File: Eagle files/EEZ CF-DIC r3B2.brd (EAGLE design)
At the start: 155 x 85 mm, 238 parts, among them IC1 MC79L05, IC2 LP2951, IC3 VIPer35L, IC4 SI8233BB-D-IS1, IC5 LM5041B, IC6 IR11688STRPBF, IC7 TL072, IC8 TL103W, IC9 TL431, P1 T910W-50K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

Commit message: X2 12V connector added
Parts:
- added X4: 39-28-1023, EEZ_Lib1:MINIFIT_5566-02A
- C4: value CY1Y-470P -> N.C.; device EEZ_Lib1:CY075-032X103 -> rcl:C0603
- C6: value N.C. -> CY1Y-470P; device rcl:C0603 -> EEZ_Lib1:CY075-032X103
- R2: value 220K -> 120R; device rcl:R1206 -> rcl:R0805
- R3: value 120R -> 220K; device rcl:R0805 -> rcl:R1206
- TP6: device EEZ_Lib1:TP_1.1MM_2 -> EEZ_Lib1:PCB_SHIELD_TAB
- TP7: device EEZ_Lib1:PCB_SHIELD_TAB -> EEZ_Lib1:TP_1.1MM_2
- X1: value 39-30-1039 -> B2B-ZR; device EEZ_Lib1:MINIFIT_39301039_CRE -> EEZ_Lib1:B2B-ZR
- X2: value 90136-1208 -> 39-30-1039; device con-molex:70543-08 -> EEZ_Lib1:MINIFIT_39301039_CRE
- X3: value 39-28-1023 -> 90136-1208; device EEZ_Lib1:MINIFIT_5566-02A -> con-molex:70543-08
- moved X2 146.6 mm to (145.0, 9.91), turned to 180 degrees
- moved R2 101.0 mm to (64.4, 83.4), flipped to the top, turned to 270 degrees
- moved R3 101.0 mm to (150.3, 30.3), flipped to the bottom, turned to 180 degrees
- moved X1 91.2 mm to (77.5, 71.2), turned to 270 degrees
- moved C4 79.1 mm to (78.1, 78.4), flipped to the bottom, turned to 180 degrees
- moved C6 69.6 mm to (143.0, 53.3), flipped to the top
- moved TP6 65.3 mm to (72.7, 39.5)
- moved TP8 38.4 mm to (34.3, 38.7)
- moved TP7 27.4 mm to (7.62, 44.5)
- moved X3 26.4 mm to (9.59, 66.1)
- moved C5 10.2 mm to (153.2, 53.3), turned to 0 degrees
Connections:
- net +12V: now also C4.1, X1.1; no longer C6.1
- net -9V: now also X3.8; no longer X2.8
- net 0V: now also C4.2, X1.2; no longer C6.2
- net DC_OUT: now also X3.3; no longer X2.3
- net FB: now also TP8.1; no longer TP7.1
- net GND: now also TP7.GND, X3.6, X4.2; no longer TP6.GND, X2.6, X3.2
- net ISO_FB: now also TP6.1; no longer TP8.1
- net N$140: now also R2.2; no longer R3.2
- net N$15: now also C6.2; no longer C5.2
- net N$24: now also C5.2; no longer C4.2
- net N$27: now also R2.1; no longer R3.1
- net N$28: now also X2.2; no longer X1.2
- net N$30: now also R3.2, X2.3; no longer R2.2, X1.3
- net N$33: now also R3.1; no longer R2.1
- net PE: now also C6.1, X2.1; no longer C4.1, X1.1
- net PREG_OUT+: now also TP7.TIP, X3.2, X4.1; no longer TP6.TIP, X2.2, X3.1
- net PWRGOOD: now also X3.4; no longer X2.4
- net U_MON: now also X3.1; no longer X2.1
- net V+: now also X3.5; no longer X2.5
- net V-: now also X3.7; no longer X2.7
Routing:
- net +12V: track 107.7 -> 114.1 mm
- net 0V: track 588.9 -> 591.1 mm
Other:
- board text added: "X3 connector"
- board text added: "X4"
- board text removed: "X2 connector"

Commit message: small changes on PCB, added alternative sync MOSFET in BOM
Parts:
- added C73: N.C., rcl:C0805
- C59: value 4n7/200V -> 100n/100V; device rcl:C1206 -> rcl:C0805
- C60, C64: value 100n -> 4n7/200V; device rcl:C0603 -> rcl:C1206
- C61: value 10u -> 100n; device rcl:C1210 -> rcl:C0603
- C62: value 100n -> 10u; device rcl:C0603 -> rcl:C1210
- C63: value 4n7/200V -> 100n; device rcl:C1206 -> rcl:C0603
- C66: value 100p -> 100n; device rcl:C0805 -> rcl:C0603
- C68: value 33n -> 100p
- C69: value 4u7 -> 33n; device EEZ_Lib1:EC1206 -> rcl:C0805
- C70: value 1u -> 4u7; device rcl:C0805 -> EEZ_Lib1:EC1206
- C71: value N.C. -> 1u
- moved C59 48.5 mm to (10.5, 44.5), turned to 180 degrees
- moved C62 44.9 mm to (33.3, 6.67), turned to 270 degrees
- moved C63 34.6 mm to (46.7, 49.5)
- moved C64 29.2 mm to (42.1, 15.2)
- moved C71 19.4 mm to (57.1, 33.9), turned to 0 degrees
- moved C66 11.7 mm to (47.2, 40.2), turned to 0 degrees
- moved R38 11.0 mm to (132.9, 75.9)
- moved R42 11.0 mm to (132.9, 71.1)
- moved C70 10.3 mm to (58.1, 44.2)
- moved C67 9.66 mm to (56.6, 47.2), turned to 270 degrees
- moved C60 8.81 mm to (39.4, 5.52), turned to 0 degrees
- moved C69 7.58 mm to (56.1, 36.9), turned to 270 degrees
- moved C65 5.86 mm to (52.6, 42.5)
- moved C68 3.15 mm to (59.1, 37.9), turned to 180 degrees
- moved C72 3.15 mm to (39.3, 41.8), turned to 270 degrees
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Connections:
- net FB: now also C72.2; no longer C71.2
- net GND: now also C66.2, C70.-, C71.2; no longer C69.-, C70.2
- net N$1: now also C67.2; no longer C66.2
- net N$10: now also C68.2; no longer C67.2
- net N$134: now also C67.1; no longer C66.1
- net N$17: now also C73.2; no longer C72.2
- net N$6: now also C62.1; no longer C60.1
- net N$66: now also C60.1; no longer C59.1
- net N$67: now also C64.1; no longer C63.1
- net N$7: now also C71.1; no longer C70.1
- net N$76: now also C69.1, C73.1; no longer C67.1, C71.1
- net N$9: now also C69.2; no longer C68.2
- net NFB_OFFSET: now also C70.+; no longer C69.+
- net PREG_OUT+: now also C59.1
- net V+: now also C63.1, C66.1; no longer C62.1, C65.1
- net V-: now also C65.1; no longer C64.1
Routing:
- net ULVO: track 67.0 -> 77.4 mm
- net DC_BUS: track 187.0 -> 179.3 mm
- net PE: track 189.6 -> 195.4 mm, vias 2 -> 3
- net GND: track 136.4 -> 137.9 mm
- net PREG_OUT+: track 56.4 -> 55.2 mm
- net N$7: track 67.3 -> 66.4 mm
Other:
- board text added: "C73"

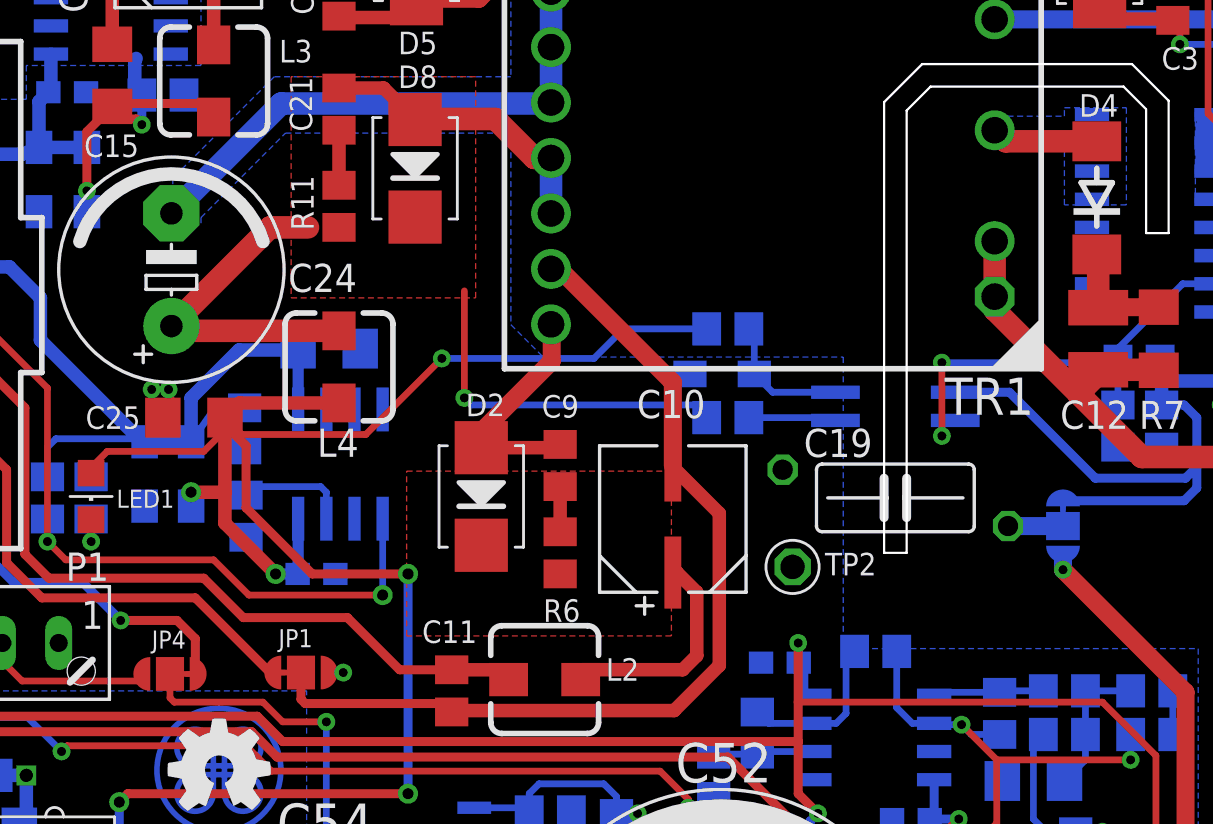
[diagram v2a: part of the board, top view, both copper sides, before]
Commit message: fixed .sch - .brd inconsistency reported by Eagle 7.x
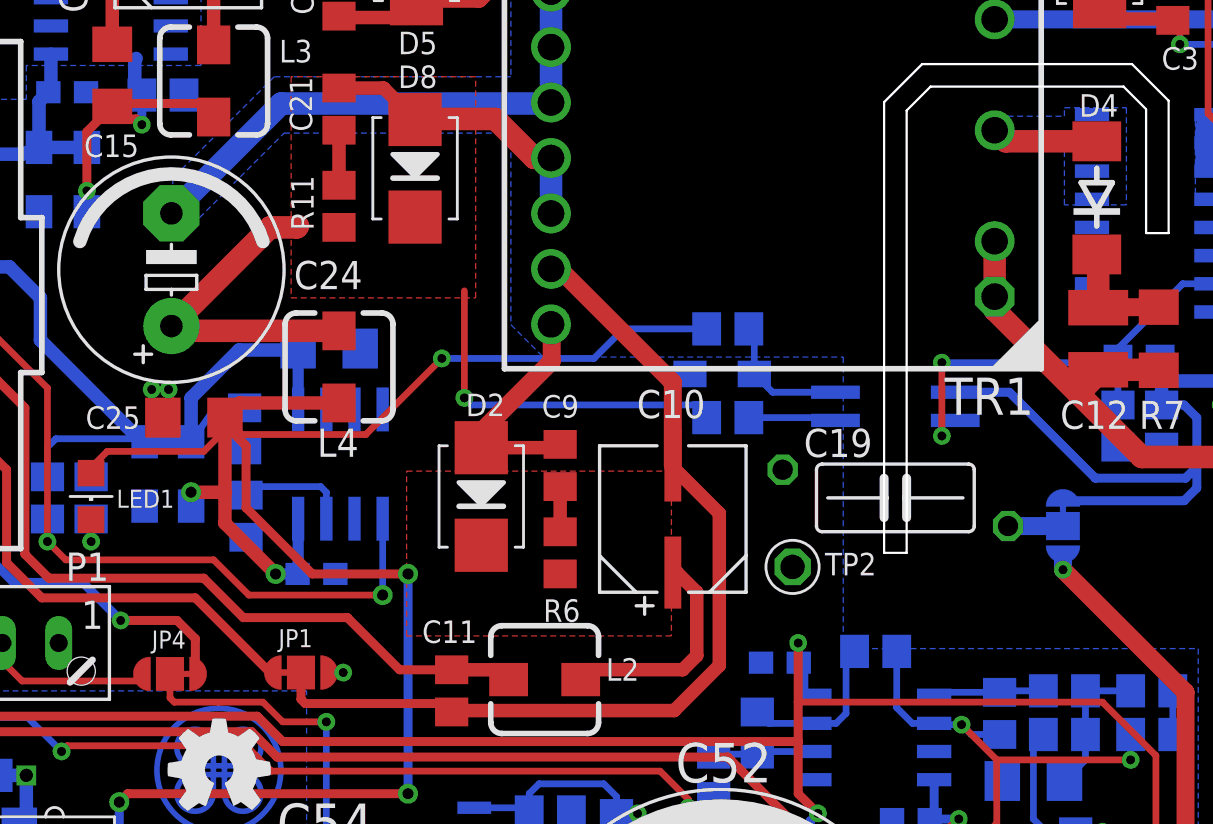
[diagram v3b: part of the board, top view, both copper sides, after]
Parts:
- TR1: value (none) -> Feryster 5572
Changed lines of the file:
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@@
 <layer number="17" name="Pads" color="14" fill="1" visible="yes" active="yes"/>
 <layer number="18" name="Vias" color="6" fill="1" visible="yes" active="yes"/>
-<layer number="19" name="Unrouted" color="6" fill="1" visible="no" active="yes"/>
+<layer number="19" name="Unrouted" color="6" fill="1" visible="yes" active="yes"/>
 <layer number="20" name="Dimension" color="4" fill="1" visible="yes" active="yes"/>
 <layer number="21" name="tPlace" color="7" fill="1" visible="yes" active="yes"/>
 <layer number="22" name="bPlace" color="6" fill="1" visible="yes" active="yes"/>
-<layer number="23" name="tOrigins" color="15" fill="1" visible="no" active="yes"/>
-<layer number="24" name="bOrigins" color="15" fill="1" visible="no" active="yes"/>
+<layer number="23" name="tOrigins" color="15" fill="1" visible="yes" active="yes"/>
+<layer number="24" name="bOrigins" color="15" fill="1" visible="yes" active="yes"/>
 <layer number="25" name="tNames" color="7" fill="1" visible="yes" active="yes"/>
-<layer number="26" name="bNames" color="5" fill="1" visible="no" active="yes"/>
+<layer number="26" name="bNames" color="5" fill="1" visible="yes" active="yes"/>
 <layer number="27" name="tValues" color="12" fill="1" visible="no" active="yes"/>
 <layer number="28" name="bValues" color="10" fill="1" visible="no" active="yes"/>
-<layer number="29" name="tStop" color="7" fill="1" visible="yes" active="yes"/>
+<layer number="29" name="tStop" color="7" fill="1" visible="no" active="yes"/>
 <layer number="30" name="bStop" color="7" fill="1" visible="no" active="yes"/>
 <layer number="31" name="tCream" color="7" fill="4" visible="no" active="yes"/>
@@
 <layer number="37" name="tTest" color="7" fill="1" visible="no" active="yes"/>
 <layer number="38" name="bTest" color="7" fill="1" visible="no" active="yes"/>
-<layer number="39" name="tKeepout" color="15" fill="1" visible="yes" active="yes"/>
+<layer number="39" name="tKeepout" color="15" fill="1" visible="no" active="yes"/>
 <layer number="40" name="bKeepout" color="5" fill="1" visible="no" active="yes"/>
 <layer number="41" name="tRestrict" color="4" fill="10" visible="no" active="yes"/>
@@
 <text x="24.257" y="52.5145" size="1.016" layer="126" ratio="10" rot="MR180">C22</text>
 <text x="24.8285" y="65.9765" size="1.016" layer="126" ratio="10" rot="MR180">C23</text>
-<text x="24.511" y="66.2432" size="1.27" layer="125" ratio="10">C24</text>
+<text x="24.765" y="66.3702" size="1.27" layer="125" ratio="10">C24</text>
 <text x="17.8435" y="61.087" size="1.016" layer="125" ratio="10" rot="R180">C25</text>
 <text x="60.7695" y="61.595" size="0.8128" layer="126" ratio="10" rot="MR270">C26</text>
@@
 <attribute name="VALUE" x="69.7865" y="73.3425" size="1.016" layer="27" ratio="10" rot="R270"/>
 </element>
-<element name="TR1" library="EEZ_inductors_and_transformers" package="FERYSTER_5572" value="" x="46.355" y="73.533" smashed="yes" rot="R180">
+<element name="TR1" library="EEZ_inductors_and_transformers" package="FERYSTER_5572" value="Feryster 5572" x="46.355" y="73.533" smashed="yes" rot="R180">
 <attribute name="NAME" x="54.102" y="60.706" size="1.6764" layer="25" ratio="10"/>
 <attribute name="VALUE" x="50.292" y="74.3585" size="1.6764" layer="27" rot="R180"/>
@@
 <attribute name="NAME" x="132.1435" y="15.9385" size="1.016" layer="25" ratio="10" rot="R180"/>
 </element>
-<element name="C24" library="EEZ_Lib1" package="ECAP5/10.5" value="470u" x="19.2405" y="67.2465" smashed="yes" rot="R90">
-<attribute name="NAME" x="24.511" y="66.2432" size="1.27" layer="25" ratio="10"/>
-<attribute name="VALUE" x="17.1958" y="66.5607" size="1.27" layer="27" ratio="10"/>
-</element>
 <element name="ZD6" library="EEZ_Lib1" package="DO214AC" value="SMAJ58A-TR" x="12.5095" y="36.8935" smashed="yes" rot="MR180">
 <attribute name="NAME" x="10.7585" y="35.6075" size="1.27" layer="26" ratio="10" rot="MR180"/>
@@
 <attribute name="VALUE" x="7.366" y="44.831" size="0.8128" layer="28" ratio="10" rot="MR180"/>
 </element>
+<element name="C24" library="EEZ_Lib1" package="ECAP5/10.5" value="470u" x="19.2405" y="67.2465" smashed="yes" rot="R90">
+<attribute name="NAME" x="24.765" y="66.3702" size="1.27" layer="25" ratio="10"/>
+<attribute name="VALUE" x="22.4663" y="64.1223" size="1.27" layer="27" ratio="10" rot="R90"/>
+</element>
 </elements>
 <signals>
@@
 <vertex x="12.446" y="40.132"/>
 </polygon>
-<contactref element="C24" pad="-"/>
-<contactref element="C24" pad="-"/>
 <wire x1="24.1935" y1="74.7395" x2="36.3115" y2="74.7395" width="1.016" layer="16"/>
 <wire x1="36.3115" y1="74.7395" x2="36.355" y2="74.783" width="1.016" layer="16"/>
-<wire x1="24.1935" y1="74.7395" x2="19.2405" y2="69.7865" width="1.016" layer="16"/>
 <polygon width="0.254" layer="16" isolate="0.3048" rank="3">
 <vertex x="5.08" y="87.122"/>
@@
 <vertex x="23.876" y="75.946"/>
 <vertex x="19.304" y="71.374"/>
-<vertex x="19.304" y="69.342"/>
-<vertex x="20.574" y="69.342"/>
-<vertex x="20.574" y="69.596"/>
-<vertex x="24.384" y="73.406"/>
+<vertex x="19.304" y="69.596"/>
+<vertex x="20.5105" y="69.596"/>
+<vertex x="24.3205" y="73.406"/>
 <vertex x="34.544" y="73.406"/>
 <vertex x="34.544" y="64.77"/>
@@
 <wire x1="12.7" y1="44.45" x2="12.7" y2="42.6055" width="0.6096" layer="16"/>
 <wire x1="12.7" y1="42.6055" x2="12.3855" y2="42.1005" width="0.6096" layer="16"/>
-<wire x1="34.3575" y1="5.842" x2="34.3535" y2="5.7785" width="0" layer="19" extent="1-1"/>
 <wire x1="12.3855" y1="42.1005" x2="12.3855" y2="41.467" width="0.6096" layer="16"/>
 <wire x1="12.3855" y1="41.467" x2="13.9745" y2="39.878" width="0.6096" layer="16"/>
+<contactref element="C24" pad="-"/>
+<wire x1="24.1935" y1="74.7395" x2="19.2405" y2="69.7865" width="1.016" layer="16"/>
+<wire x1="34.3535" y1="5.7785" x2="34.3575" y2="5.842" width="0" layer="19" extent="1-1"/>
 </signal>
 <signal name="REF">
@@
 <vertex x="32.9565" y="75.946"/>
 </polygon>
-<contactref element="C24" pad="+"/>
-<wire x1="23.688" y1="69.154" x2="19.2405" y2="64.7065" width="1.016" layer="1"/>
 <wire x1="26.797" y1="64.491" x2="19.456" y2="64.491" width="1.016" layer="1"/>
-<wire x1="19.456" y1="64.491" x2="19.2405" y2="64.7065" width="1.016" layer="1"/>
 <wire x1="43.373" y1="60.579" x2="43.373" y2="61.148" width="0.3048" layer="16"/>
 <wire x1="43.373" y1="61.148" x2="43.3705" y2="61.1505" width="0.3048" layer="16"/>
@@
 <wire x1="32.766" y1="61.1505" x2="32.4485" y2="61.468" width="0.3048" layer="16"/>
 <contactref element="R11" pad="1"/>
-<wire x1="23.688" y1="69.154" x2="25.4" y2="69.154" width="1.016" layer="1"/>
-<wire x1="25.4" y1="69.154" x2="25.4" y2="69.215" width="0.8128" layer="1"/>
+<contactref element="C24" pad="+"/>
+<wire x1="23.688" y1="69.154" x2="19.2405" y2="64.7065" width="1.016" layer="1"/>
+<wire x1="19.456" y1="64.491" x2="19.2405" y2="64.7065" width="1.016" layer="1"/>
+<wire x1="23.688" y1="69.154" x2="24.8945" y2="69.154" width="1.016" layer="1"/>
+<wire x1="24.8945" y1="69.154" x2="24.9555" y2="69.215" width="1.016" layer="1"/>
 </signal>
 <signal name="N$136">
